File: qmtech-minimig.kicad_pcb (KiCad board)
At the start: 4 copper layers, 16 x 0.6 mm, 120 parts, among them IC1 RTL8211EG-VB-CG, J1 DB9_Male, J2 DB9_Male, J3 SCHA5B0200, J4 ARM_JTAG, J5 AUDIO-CONNECTOR-6P-SMD-344003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, J6 Mini-DIN-6, J7 HDMI_D_1.4, J8 HR911130A, SW1 SW_Push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

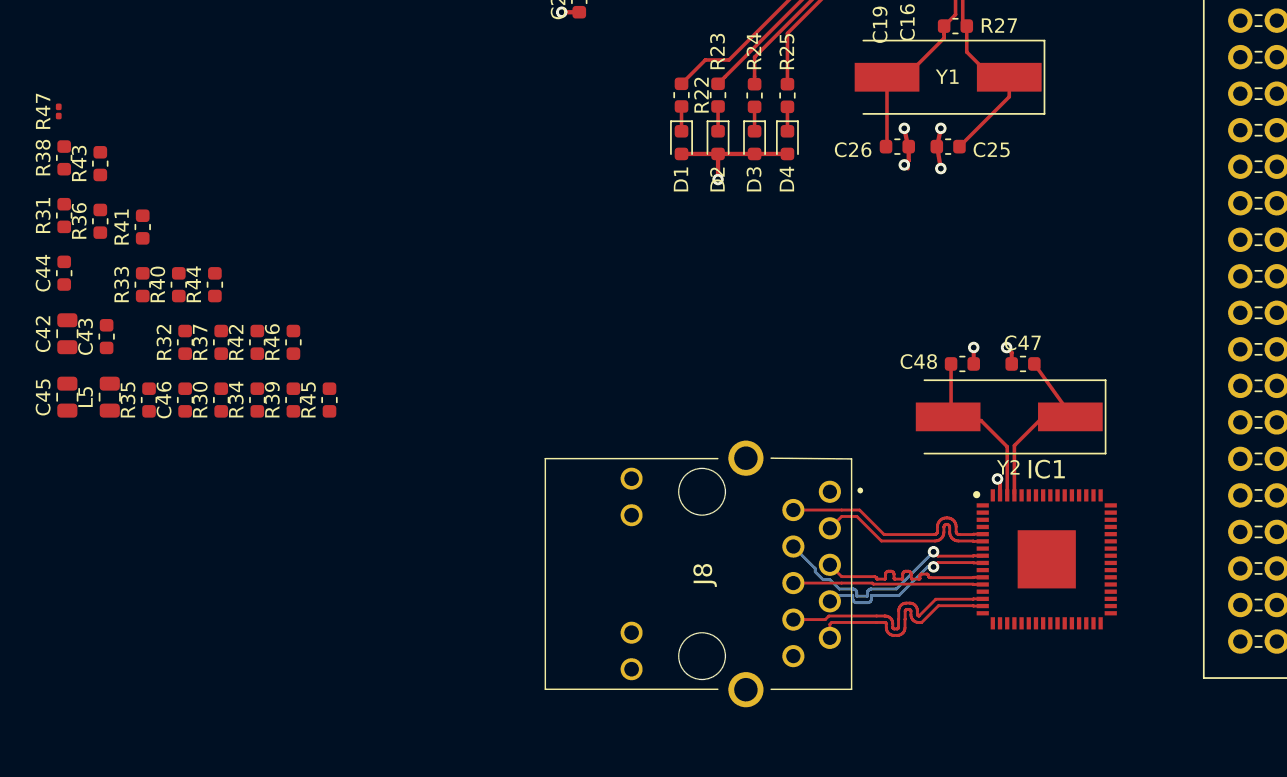
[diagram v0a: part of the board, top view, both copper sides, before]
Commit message: Wired the RTL8211EG more.
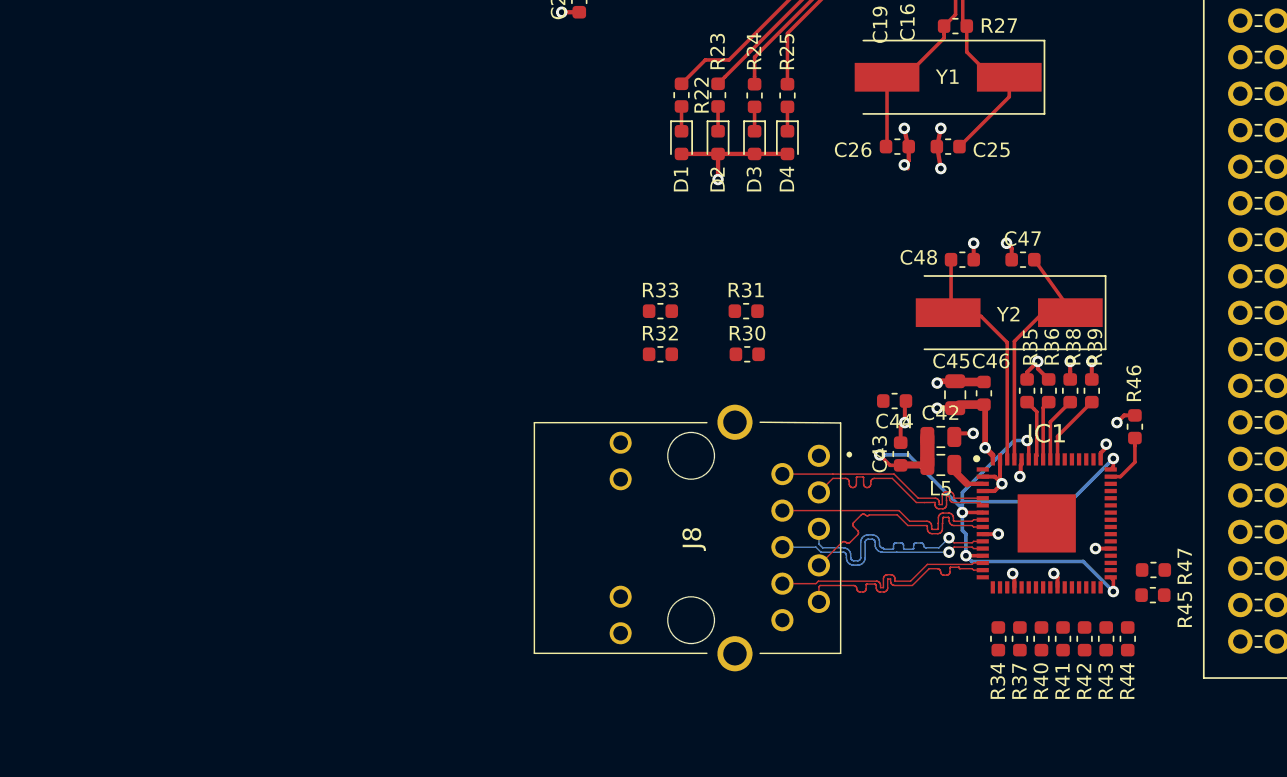
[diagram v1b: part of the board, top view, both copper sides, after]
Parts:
- R47: footprint Resistor_SMD:R_0201_0603Metric -> Resistor_SMD:R_0603_1608Metric
- moved R47 82.5 mm to (94.3, 144.2), turned to 180 degrees
- moved R43 77.4 mm to (91.0, 149.0), turned to 270 degrees
- moved R38 71.8 mm to (88.5, 131.8)
- moved R41 70.1 mm to (88.0, 149.0), turned to 270 degrees
- moved R44 68.1 mm to (92.5, 149.0), turned to 270 degrees
- moved R36 67.0 mm to (87.0, 131.8)
- moved R40 64.9 mm to (86.5, 149.0), turned to 270 degrees
- moved C45 61.7 mm to (80.5, 132.1)
- moved C42 61.2 mm to (79.5, 135.0), turned to 0 degrees
- moved R42 61.1 mm to (89.5, 149.0), turned to 270 degrees
- moved R35 61.1 mm to (85.5, 131.8)
- moved R37 59.2 mm to (85.0, 149.0), turned to 270 degrees
- moved R45 58.9 mm to (94.2, 146.0), turned to 0 degrees
- moved R46 58.8 mm to (93.0, 134.3)
- moved C44 58.4 mm to (76.3, 132.5), turned to 180 degrees
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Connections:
- net ADV_CEC renamed Net-(ADV7511KSTZ1-Pad48)
- net ADV_CEC_CLK renamed Net-(ADV7511KSTZ1-Pad50)
- ADV7511KSTZ1 pad 29: ADV_AVDD -> Net-(ADV7511KSTZ1-Pad29)
- ADV7511KSTZ1 pad 32: ADV_TXC- -> Net-(ADV7511KSTZ1-Pad32)
- ADV7511KSTZ1 pad 33: ADV_TXC+ -> Net-(ADV7511KSTZ1-Pad33)
- ADV7511KSTZ1 pad 34: ADV_AVDD -> Net-(ADV7511KSTZ1-Pad34)
- ADV7511KSTZ1 pad 35: ADV_TX0- -> Net-(ADV7511KSTZ1-Pad35)
- ADV7511KSTZ1 pad 36: ADV_TX0+ -> Net-(ADV7511KSTZ1-Pad36)
- ADV7511KSTZ1 pad 39: ADV_TX1- -> Net-(ADV7511KSTZ1-Pad39)
- ADV7511KSTZ1 pad 40: ADV_TX1+ -> Net-(ADV7511KSTZ1-Pad40)
- ADV7511KSTZ1 pad 42: ADV_TX2- -> Net-(ADV7511KSTZ1-Pad42)
- ADV7511KSTZ1 pad 43: ADV_TX2+ -> Net-(ADV7511KSTZ1-Pad43)
- ADV7511KSTZ1 pad 51: ADV_HEAC- -> Net-(ADV7511KSTZ1-Pad51)
- ADV7511KSTZ1 pad 52: ADV_HEAC+ -> Net-(ADV7511KSTZ1-Pad52)
- C42 pad 2: Net-(C42-Pad2) -> GND
- C43 pad 2: Net-(C43-Pad2) -> GND
- U2 pad U710: ADV_R_6 -> Net-(U2-PadU710)
- U2 pad U712: ADV_R_5 -> Net-(U2-PadU712)
- U2 pad U714: ADV_R_4 -> Net-(U2-PadU714)
- U2 pad U716: ADV_R_3 -> Net-(U2-PadU716)
- U2 pad U718: ADV_R_2 -> Net-(U2-PadU718)
- U2 pad U720: ADV_R_1 -> Net-(U2-PadU720)
- U2 pad U722: ADV_R_0 -> Net-(U2-PadU722)
- U2 pad U724: ADV_G_7 -> Net-(U2-PadU724)
- U2 pad U726: ADV_G_6 -> Net-(U2-PadU726)
- U2 pad U728: ADV_G_5 -> Net-(U2-PadU728)
- U2 pad U730: ADV_G_4 -> Net-(U2-PadU730)
- U2 pad U732: ADV_G_3 -> Net-(U2-PadU732)
- U2 pad U734: ADV_G_2 -> Net-(U2-PadU734)
- U2 pad U78: ADV_R_7 -> Net-(U2-PadU78)
- U2 pad U810: JS1_9 -> Net-(U2-PadU810)
- U2 pad U812: JS1_4 -> Net-(U2-PadU812)
- U2 pad U814: JS1_3 -> Net-(U2-PadU814)
- U2 pad U816: JS1_7 -> Net-(U2-PadU816)
- U2 pad U818: JS1_2 -> Net-(U2-PadU818)
- U2 pad U820: JS1_6 -> Net-(U2-PadU820)
- U2 pad U822: JS1_1 -> Net-(U2-PadU822)
- U2 pad U827: ADV_G_0 -> Net-(U2-PadU827)
- U2 pad U829: ADV_CLK -> Net-(U2-PadU829)
- U2 pad U830: JS2_5 -> Net-(U2-PadU830)
- U2 pad U831: ADV_G_1 -> Net-(U2-PadU831)
- U2 pad U832: JS2_9 -> Net-(U2-PadU832)
- U2 pad U834: JS2_4 -> Net-(U2-PadU834)
- U2 pad U836: JS2_3 -> Net-(U2-PadU836)
- U2 pad U838: JS2_7 -> Net-(U2-PadU838)
- U2 pad U840: JS2_2 -> Net-(U2-PadU840)
- U2 pad U842: JS2_6 -> Net-(U2-PadU842)
- U2 pad U844: JS2_1 -> Net-(U2-PadU844)
- U2 pad U858: PS2_CLK1 -> Net-(U2-PadU858)
- U2 pad U860: PS2_DAT1 -> Net-(U2-PadU860)
- U2 pad U88: JS1_5 -> Net-(U2-PadU88)
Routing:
- net ETH_REG_OUT_OUT: track 0.00 -> 52.2 mm, vias 0 -> 6
- net GND: track 160.4 -> 177.8 mm, vias 52 -> 58
- net 3V3: track 60.6 -> 75.9 mm, vias 26 -> 35
- net Net-(IC1-Pad55): track 0.00 -> 4.97 mm
- net ETH_CKXTAL2: track 12.4 -> 17.2 mm
- net ETH_CKXTAL1: track 12.7 -> 17.5 mm
- net Net-(IC1-Pad56): track 0.00 -> 4.56 mm
- net Net-(IC1-Pad58): track 0.00 -> 4.29 mm
- net Net-(IC1-Pad57): track 0.00 -> 4.14 mm
- net Net-(IC1-Pad47): track 0.00 -> 3.78 mm
- net ETH_MDI_2+: track 13.2 -> 17.0 mm, vias 0 -> 1
- net ETH_MDI_2-: track 13.2 -> 16.9 mm, vias 0 -> 1
- net ETH_MDI_1-: track 12.5 -> 16.0 mm, vias 2 -> 0
- net ETH_MDI_0-: track 13.3 -> 16.1 mm
- net ETH_REG_OUT: track 0.00 -> 2.23 mm
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
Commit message: Fixed wiring ad7511 and wired the rtl8211EG IC
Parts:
- moved R44 17.6 mm to (93.2, 131.5), turned to 315 degrees
- moved R45 16.8 mm to (94.3, 129.2)
- moved C47 16.7 mm to (69.8, 116.2), turned to 45 degrees
- moved R47 16.6 mm to (94.3, 127.7)
- moved R39 16.2 mm to (79.7, 119.2), turned to 135 degrees
- moved R46 16.1 mm to (87.4, 119.2), turned to 45 degrees
- moved R38 15.1 mm to (78.6, 120.4), turned to 135 degrees
- moved Y2 15.1 mm to (70.2, 120.8), turned to 225 degrees
- moved C48 14.9 mm to (66.4, 119.6), turned to 225 degrees
- moved R43 14.5 mm to (94.5, 134.9), turned to 315 degrees
- moved R36 14.1 mm to (77.5, 121.5), turned to 135 degrees
- moved R42 13.2 mm to (93.1, 136.3), turned to 315 degrees
- moved IC1 13.2 mm to (83.9, 128.2), turned to 45 degrees
- moved R35 13.0 mm to (76.3, 122.6), turned to 135 degrees
- moved D1 12.3 mm to (61.2, 102.2), turned to 180 degrees
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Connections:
- net Net-(IC1-Pad53) renamed ETH_MDC
- ADV7511KSTZ1 pad 29: Net-(ADV7511KSTZ1-Pad29) -> ADV_AVDD
- ADV7511KSTZ1 pad 32: Net-(ADV7511KSTZ1-Pad32) -> ADV_TXC-
- ADV7511KSTZ1 pad 33: Net-(ADV7511KSTZ1-Pad33) -> ADV_TXC+
- ADV7511KSTZ1 pad 34: Net-(ADV7511KSTZ1-Pad34) -> ADV_AVDD
- ADV7511KSTZ1 pad 35: Net-(ADV7511KSTZ1-Pad35) -> ADV_TX0-
- ADV7511KSTZ1 pad 36: Net-(ADV7511KSTZ1-Pad36) -> ADV_TX0+
- ADV7511KSTZ1 pad 39: Net-(ADV7511KSTZ1-Pad39) -> ADV_TX1-
- ADV7511KSTZ1 pad 40: Net-(ADV7511KSTZ1-Pad40) -> ADV_TX1+
- ADV7511KSTZ1 pad 42: Net-(ADV7511KSTZ1-Pad42) -> ADV_TX2-
- ADV7511KSTZ1 pad 43: Net-(ADV7511KSTZ1-Pad43) -> ADV_TX2+
- C1 pad 2: VDD3V3 -> 3V3
- C10 pad 2: VDD3V3 -> 3V3
- C11 pad 2: VDD3V3 -> 3V3
- C12 pad 2: VDD3V3 -> 3V3
- C13 pad 2: VDD3V3 -> 3V3
- C16 pad 2: VDD3V3 -> 3V3
- C17 pad 2: VDD3V3 -> 3V3
- C2 pad 2: VDD3V3 -> 3V3
- C20 pad 2: VDD3V3 -> 3V3
- C3 pad 2: VDD3V3 -> 3V3
- C4 pad 2: VDD3V3 -> 3V3
- C40 pad 1: ADV_AVDD -> GND
- C40 pad 2: GND -> ADV_AVDD
- C41 pad 1: ADV_AVDD -> GND
- C41 pad 2: GND -> ADV_AVDD
- C5 pad 2: VDD3V3 -> 3V3
- C6 pad 2: VDD3V3 -> 3V3
- C7 pad 2: VDD3V3 -> 3V3
- C8 pad 2: VDD3V3 -> 3V3
- C9 pad 2: VDD3V3 -> 3V3
- IC1 pad 18: Net-(IC1-Pad18) -> ETH_RXDV
- IC1 pad 19: Net-(IC1-Pad19) -> ETH_RXD0
- IC1 pad 21: Net-(IC1-Pad21) -> ETH_RXD1
- IC1 pad 22: Net-(IC1-Pad22) -> ETH_RXD2
- IC1 pad 23: Net-(IC1-Pad23) -> ETH_RXD3
- IC1 pad 24: Net-(IC1-Pad24) -> ETH_RXC
- IC1 pad 25: Net-(IC1-Pad25) -> ETH_RXD4
- IC1 pad 27: Net-(IC1-Pad27) -> ETH_RXD5
- IC1 pad 28: Net-(IC1-Pad28) -> ETH_RXD6
- IC1 pad 29: Net-(IC1-Pad29) -> ETH_RXD7
- IC1 pad 30: Net-(IC1-Pad30) -> ETH_RXER
- IC1 pad 31: Net-(IC1-Pad31) -> ETH_COL_MODE
- IC1 pad 32: Net-(IC1-Pad32) -> ETH_CRS
- IC1 pad 47: Net-(IC1-Pad47) -> ETH_TXER
- IC1 pad 54: Net-(IC1-Pad54) -> ETH_MDIO
- IC1 pad 56: Net-(IC1-Pad56) -> ETH_INTB
- R34 pad 1: Net-(IC1-Pad18) -> ETH_RXDV
- R37 pad 1: Net-(IC1-Pad25) -> ETH_RXD4
- R38 pad 1: Net-(IC1-Pad56) -> ETH_INTB
- R40 pad 1: Net-(IC1-Pad27) -> ETH_RXD5
- R41 pad 1: Net-(IC1-Pad28) -> ETH_RXD6
- R42 pad 1: Net-(IC1-Pad29) -> ETH_RXD7
- R43 pad 1: Net-(IC1-Pad30) -> ETH_RXER
- R44 pad 1: Net-(IC1-Pad31) -> ETH_COL_MODE
- R45 pad 1: Net-(IC1-Pad32) -> ETH_CRS
- R46 pad 1: Net-(IC1-Pad47) -> ETH_TXER
- U2 pad U710: Net-(U2-PadU710) -> ADV_R_6
- U2 pad U712: Net-(U2-PadU712) -> ADV_R_5
- U2 pad U714: Net-(U2-PadU714) -> ADV_R_4
- U2 pad U716: Net-(U2-PadU716) -> ADV_R_3
- U2 pad U718: Net-(U2-PadU718) -> ADV_R_2
- U2 pad U720: Net-(U2-PadU720) -> ADV_R_1
- U2 pad U722: Net-(U2-PadU722) -> ADV_R_0
- U2 pad U724: Net-(U2-PadU724) -> ADV_G_7
- U2 pad U726: Net-(U2-PadU726) -> ADV_G_6
- U2 pad U728: Net-(U2-PadU728) -> ADV_G_5
- U2 pad U730: Net-(U2-PadU730) -> ADV_G_4
- U2 pad U731: Net-(U2-PadU731) -> ETH_INTB
- U2 pad U732: Net-(U2-PadU732) -> ADV_G_3
- U2 pad U733: Net-(U2-PadU733) -> ETH_MDIO
- U2 pad U734: Net-(U2-PadU734) -> ADV_G_2
- U2 pad U735: Net-(U2-PadU735) -> ETH_TXER
- U2 pad U736: Net-(U2-PadU736) -> ETH_TXD7
- U2 pad U737: Net-(U2-PadU737) -> ETH_TXD6
- U2 pad U738: Net-(U2-PadU738) -> ETH_TXD5
- U2 pad U739: Net-(U2-PadU739) -> ETH_TXD4
- U2 pad U740: Net-(U2-PadU740) -> ETH_TXDCLK
- U2 pad U741: Net-(U2-PadU741) -> ETH_TXD3
- U2 pad U742: Net-(U2-PadU742) -> ETH_TXD2
- U2 pad U743: Net-(U2-PadU743) -> ETH_TXD1
- U2 pad U744: Net-(U2-PadU744) -> ETH_PHYRSTB
- U2 pad U745: Net-(U2-PadU745) -> ETH_TXD0
- U2 pad U746: Net-(U2-PadU746) -> ETH_TXEN
- U2 pad U747: Net-(U2-PadU747) -> ETH_GTX_CLK
- U2 pad U748: Net-(U2-PadU748) -> ETH_CRS
- U2 pad U749: Net-(U2-PadU749) -> ETH_COL_MODE
- U2 pad U750: Net-(U2-PadU750) -> ETH_RXER
- U2 pad U751: Net-(U2-PadU751) -> ETH_RXD7
- U2 pad U752: Net-(U2-PadU752) -> ETH_RXD6
- U2 pad U753: Net-(U2-PadU753) -> ETH_RXD5
- U2 pad U754: Net-(U2-PadU754) -> ETH_RXD4
- U2 pad U755: Net-(U2-PadU755) -> ETH_RXC
- U2 pad U756: Net-(U2-PadU756) -> ETH_RXD3
- U2 pad U757: Net-(U2-PadU757) -> ETH_RXD2
- U2 pad U758: Net-(U2-PadU758) -> ETH_RXD1
- U2 pad U759: Net-(U2-PadU759) -> ETH_RXD0
- U2 pad U760: Net-(U2-PadU760) -> ETH_RXDV
- U2 pad U78: Net-(U2-PadU78) -> ADV_R_7
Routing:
- net Net-(ADV7511KSTZ1-Pad52): track 0.00 -> 37.5 mm
- net ADV_HEAC+: track 37.5 -> 0.00 mm
- net Net-(ADV7511KSTZ1-Pad51): track 0.00 -> 37.3 mm
- net ADV_HEAC-: track 37.3 -> 0.00 mm
- net ETH_LED0: track 0.00 -> 35.2 mm, vias 0 -> 2
- net ETH_LED1: track 0.00 -> 34.3 mm, vias 0 -> 2
- net ETH_INTB: track 0.00 -> 30.9 mm, vias 0 -> 1
- net ETH_RXDV: track 0.00 -> 26.8 mm
- net ETH_RXD4: track 0.00 -> 26.7 mm
- net ETH_MDIO: track 0.00 -> 26.1 mm
- net ETH_RXD1: track 0.00 -> 23.7 mm, vias 0 -> 1
- net Net-(J8-Pad11): track 0.00 -> 22.8 mm
- net ETH_RXD0: track 0.00 -> 22.3 mm
- net ETH_TXD7: track 0.00 -> 22.0 mm
- net ETH_RXD3: track 0.00 -> 21.8 mm, vias 0 -> 1
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
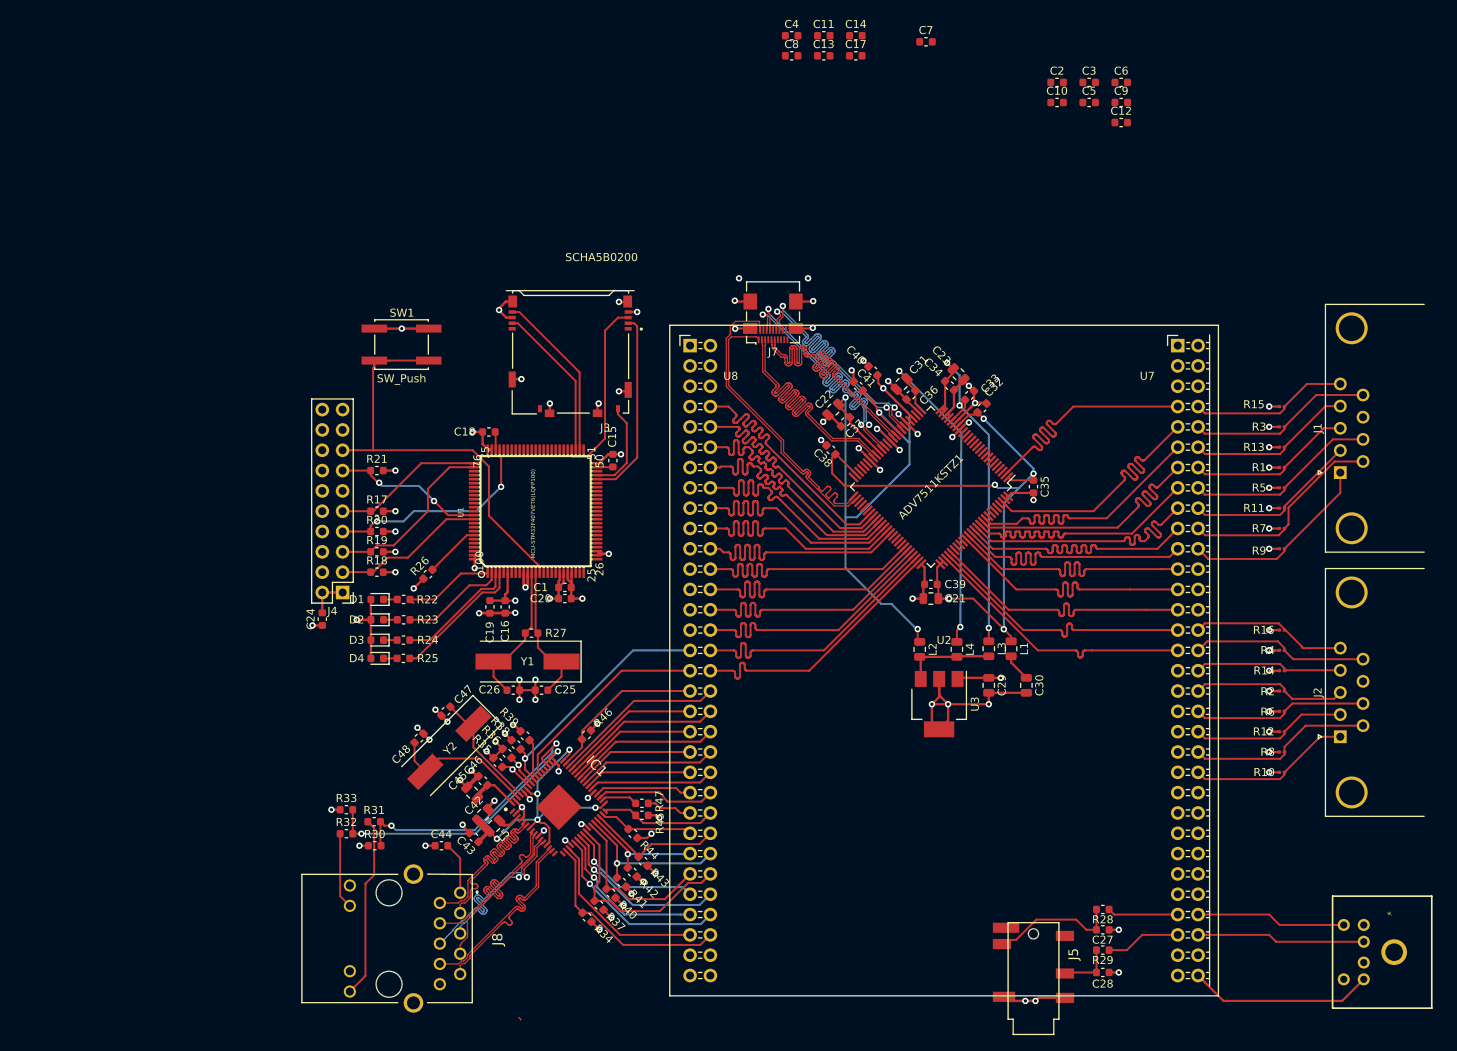
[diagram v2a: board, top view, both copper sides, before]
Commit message: Moved to full size HDMI.
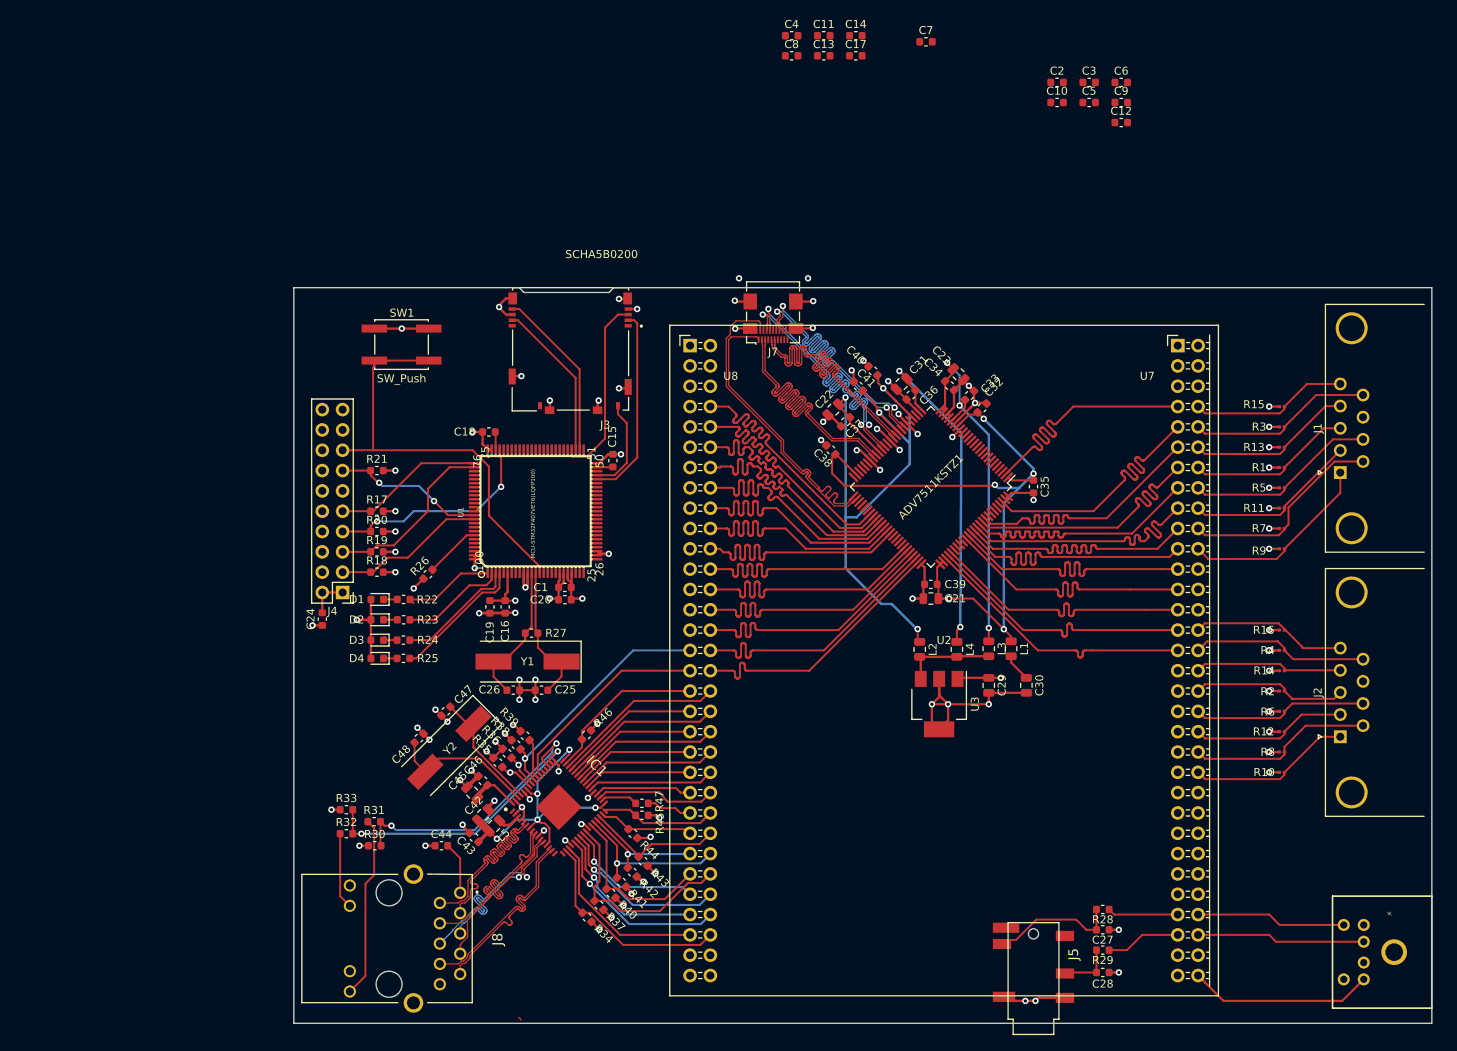
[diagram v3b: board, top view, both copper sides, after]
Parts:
- moved J3 0.38 mm to (85.3, 70.7)
- moved C20 0.14 mm to (84.7, 102.2)
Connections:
- ADV7511KSTZ1 pad 51: Net-(ADV7511KSTZ1-Pad51) -> ADV_HEAC-
- ADV7511KSTZ1 pad 52: Net-(ADV7511KSTZ1-Pad52) -> ADV_HEAC+
- U2 pad U810: Net-(U2-PadU810) -> JS1_9
- U2 pad U812: Net-(U2-PadU812) -> JS1_4
- U2 pad U814: Net-(U2-PadU814) -> JS1_3
- U2 pad U816: Net-(U2-PadU816) -> JS1_7
- U2 pad U818: Net-(U2-PadU818) -> JS1_2
- U2 pad U820: Net-(U2-PadU820) -> JS1_6
- U2 pad U822: Net-(U2-PadU822) -> JS1_1
- U2 pad U827: Net-(U2-PadU827) -> ADV_G_0
- U2 pad U829: Net-(U2-PadU829) -> ADV_CLK
- U2 pad U830: Net-(U2-PadU830) -> JS2_5
- U2 pad U831: Net-(U2-PadU831) -> ADV_G_1
- U2 pad U832: Net-(U2-PadU832) -> JS2_9
- U2 pad U834: Net-(U2-PadU834) -> JS2_4
- U2 pad U836: Net-(U2-PadU836) -> JS2_3
- U2 pad U838: Net-(U2-PadU838) -> JS2_7
- U2 pad U840: Net-(U2-PadU840) -> JS2_2
- U2 pad U842: Net-(U2-PadU842) -> JS2_6
- U2 pad U844: Net-(U2-PadU844) -> JS2_1
- U2 pad U858: Net-(U2-PadU858) -> PS2_CLK1
- U2 pad U860: Net-(U2-PadU860) -> PS2_DAT1
- U2 pad U88: Net-(U2-PadU88) -> JS1_5
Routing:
- net Net-(ADV7511KSTZ1-Pad52): track 37.5 -> 0.00 mm
- net ADV_HEAC+: track 0.00 -> 37.4 mm
- net Net-(ADV7511KSTZ1-Pad51): track 37.3 -> 0.00 mm
- net ADV_HEAC-: track 0.00 -> 37.3 mm
- net GND: track 185.2 -> 184.6 mm, vias 67 -> 66
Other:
- board size 16 x 0.6 mm -> 142.2 x 92 mm
